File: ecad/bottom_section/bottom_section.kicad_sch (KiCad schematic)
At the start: 13 parts, among them J1 JST PH, J2 JST SH, J3 JST PH, U1 MCP23017_ML

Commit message: Adds a bottom_section board.
It was fast. Seems the right design choices.
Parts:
- removed J1, J3: JST PH, Connector_JST:JST_PH_S4B-PH-K_1x04_P2.00mm_Horizontal, symbol Connector_Generic:Conn_01x04
- added J1, J3: JST PH, Connector_JST:JST_PH_S3B-PH-K_1x03_P2.00mm_Horizontal, symbol Connector_Generic:Conn_01x03
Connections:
- net R6_S6 is gone; now on net R5_SW: U1.18 (GPA1)
- net +5V: now also J1.3 (Pin_3), J3.3 (Pin_3)
- net DIN: now also R8.1, J1.2 (Pin_2); no longer R7.1
- net DOUT: now also R7.1, J3.2 (Pin_2); no longer R8.1
- net GND: now also J1.1 (Pin_1), J3.1 (Pin_1)
- net KeyboardKey_COL1/DIN: no longer R7.2
- net KeyboardKey_COL10/DOUT: now also R7.2
- net KeyboardKey_COL6/DOUT: no longer R8.2
- net R5_SW: no longer U1.17 (GPA0)
- net R6_SW: now also U1.17 (GPA0)
- new net KeyboardKey_COL5/DIN: R8.2
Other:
- moved on the sheet: R7, R8

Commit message: Updates boards
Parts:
- removed R2, R3, R4, R5, R6: 11k, Resistor_SMD:R_0603_1608Metric, symbol Device:R
- added JP1, JP2, JP3: ~, Jumper:SolderJumper-3_P2.0mm_Open_TrianglePad1.0x1.5mm, symbol Jumper:SolderJumper_3_Bridged123
- J1, J3: value JST PH -> JST PH 3; footprint Connector_JST:JST_PH_S3B-PH-K_1x03_P2.00mm_Horizontal -> woodpecker:JST_PH_S3B-PH-SM4-TB_1x03-1MP_P2.00mm_Horizontal
- J2: value JST SH -> JST SH 4; footprint Connector_JST:JST_SH_BM04B-SRSS-TB_1x04-1MP_P1.00mm_Vertical -> woodpecker:JST_SH_BM04B-SRSS-TB_1x04-1MP_P1.00mm_Vertical
- R1: now fitted
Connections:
- net A0: now also JP1.2 (C)
- net A1: now also JP2.2 (C)
- net A2: now also JP3.2 (C); no longer R1.2
- net GND: now also JP1.3 (B), JP2.3 (B), JP3.3 (B)
- new net 3v3_PUP: JP1.1 (A), JP2.1 (A), JP3.1 (A), R1.2

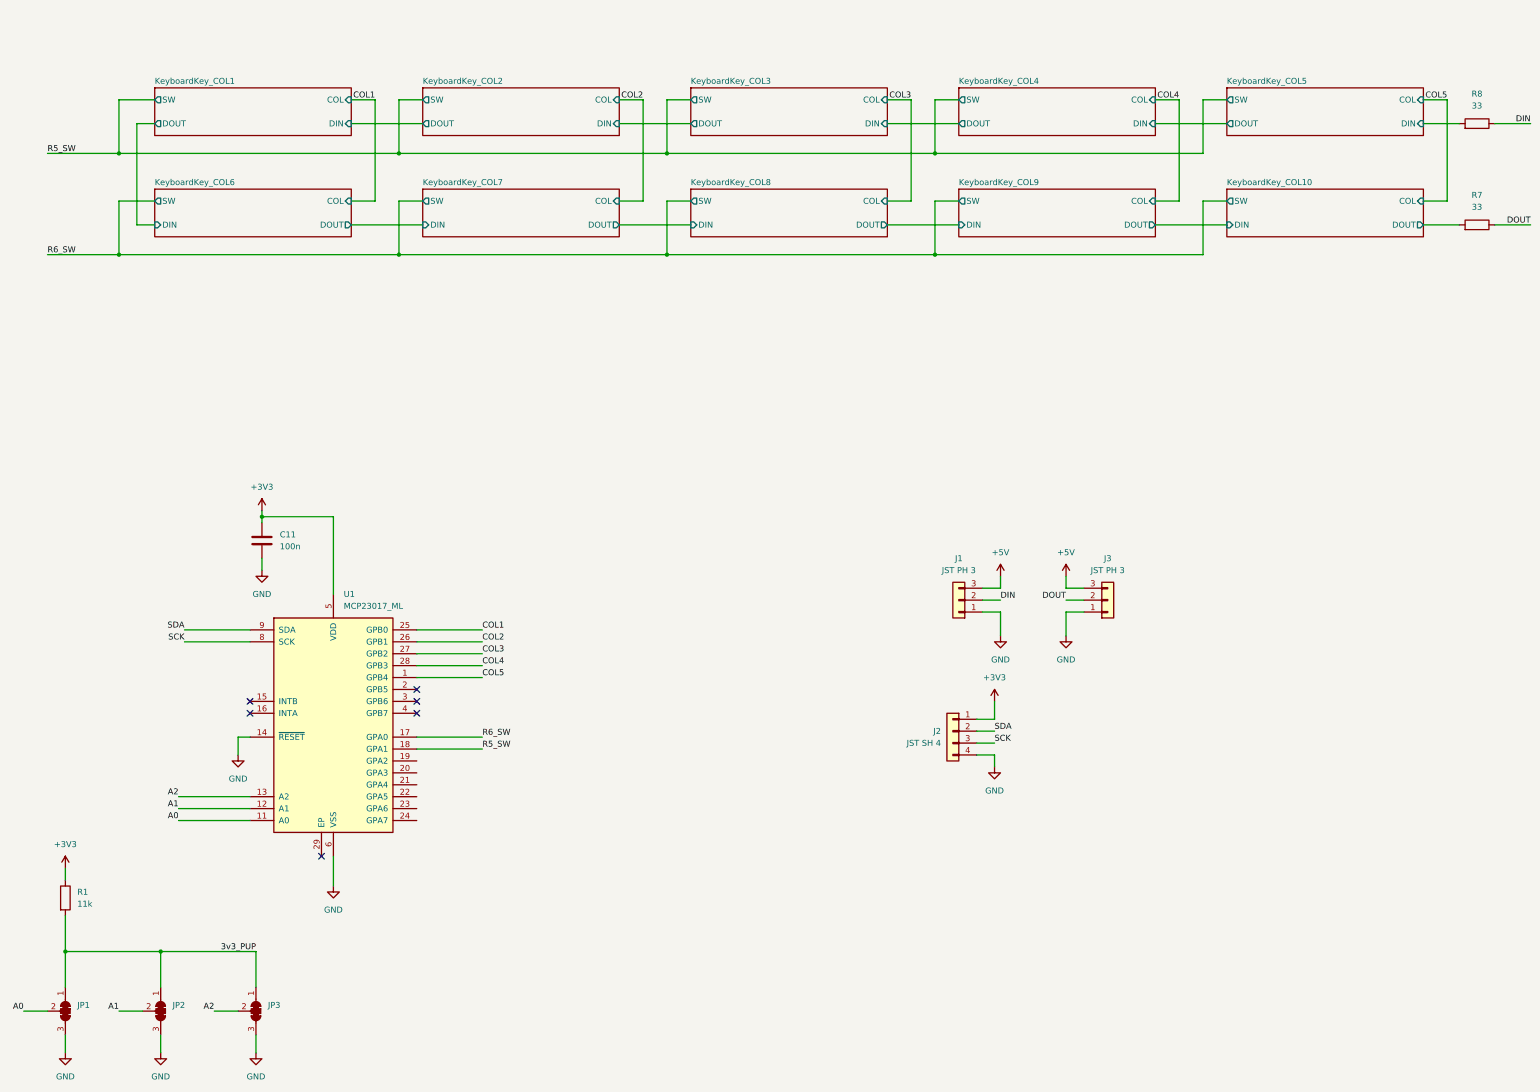
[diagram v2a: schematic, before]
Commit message: Uses Attiny1617 MCU for ADC & Matrix RO
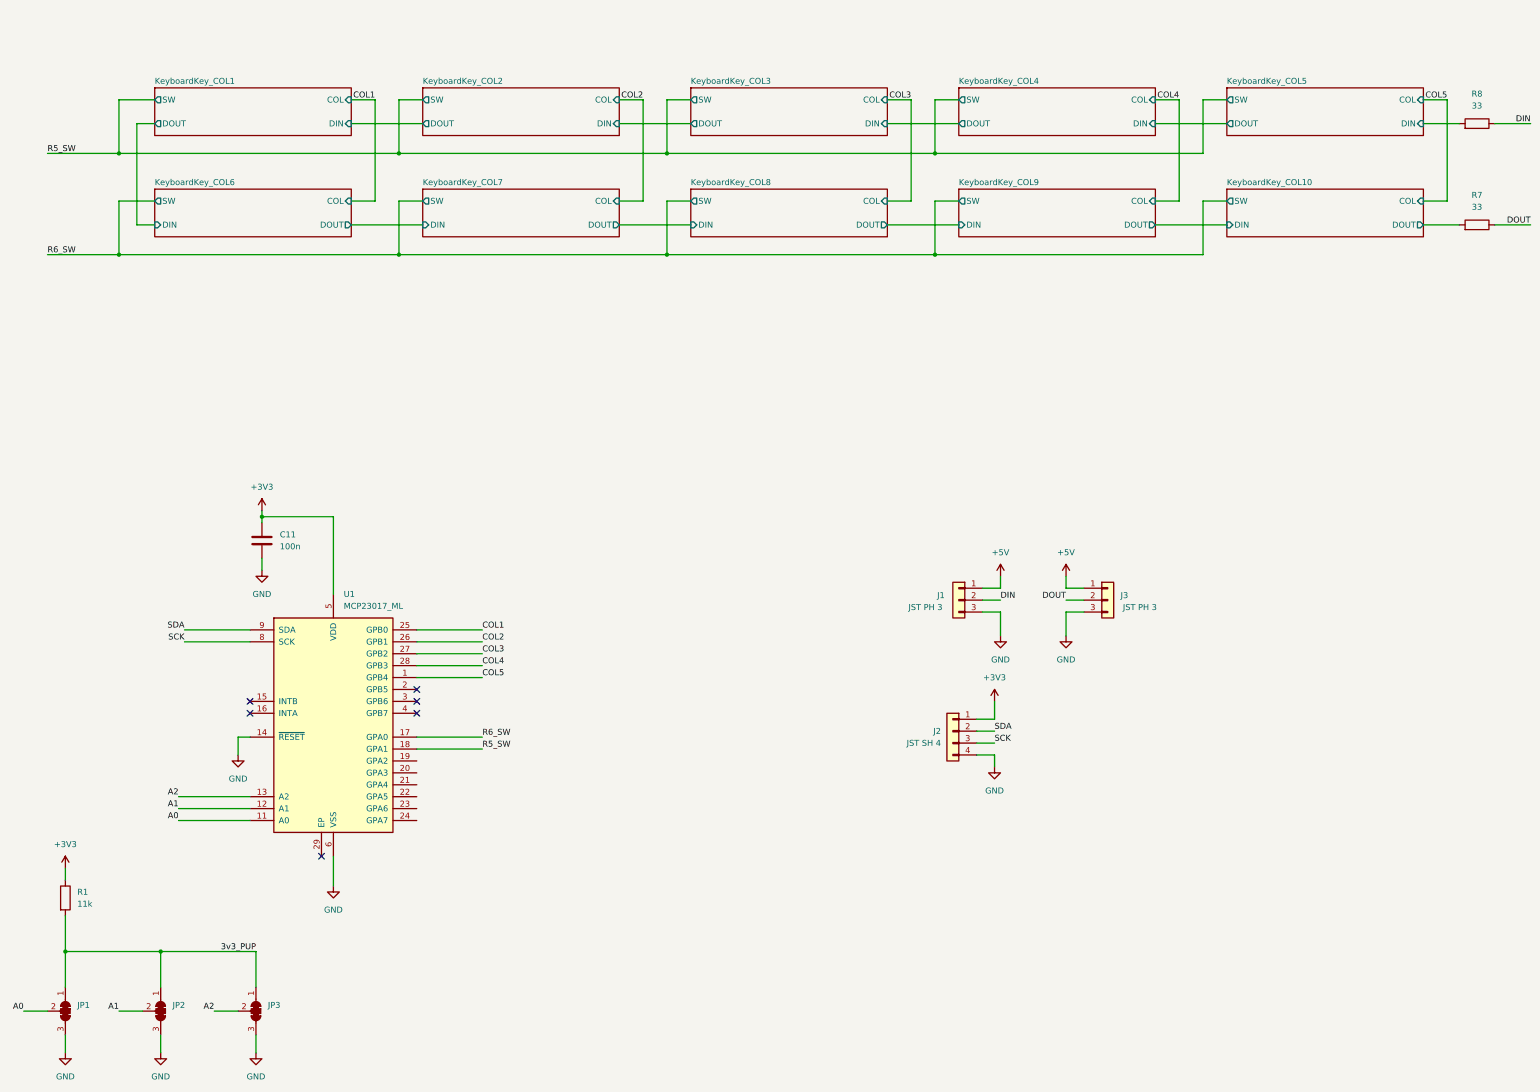
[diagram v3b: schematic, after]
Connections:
- net +5V: now also J1.1 (Pin_1), J3.1 (Pin_1); no longer J1.3 (Pin_3), J3.3 (Pin_3)
- net GND: now also J1.3 (Pin_3), J3.3 (Pin_3); no longer J1.1 (Pin_1), J3.1 (Pin_1)
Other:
- moved on the sheet: J1
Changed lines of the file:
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@@
 (kicad_sch
-	(version 20231120)
+	(version 20250114)
 	(generator "eeschema")
-	(generator_version "8.0")
+	(generator_version "9.0")
 	(paper "A3")
 	(junction
@@
 	(label "COL4"
 		(at 285.75 40.64 180)
-		(fields_autoplaced yes)
 		(effects
 			(font
@@
 	(label "DIN"
 		(at 247.65 147.32 0)
-		(fields_autoplaced yes)
 		(effects
 			(font
@@
 	(label "COL3"
 		(at 228.6 40.64 180)
-		(fields_autoplaced yes)
 		(effects
 			(font
@@
 	(label "DOUT"
 		(at 360.68 67.31 180)
-		(fields_autoplaced yes)
 		(effects
 			(font
@@
 	(label "A1"
 		(at 59.69 234.95 180)
-		(fields_autoplaced yes)
 		(effects
 			(font
@@
 	(label "3v3_PUP"
 		(at 88.9 222.25 180)
-		(fields_autoplaced yes)
 		(effects
 			(font
@@
 	(label "COL4"
 		(at 137.16 161.29 0)
-		(fields_autoplaced yes)
 		(effects
 			(font
@@
 	(label "A2"
 		(at 72.39 189.23 180)
-		(fields_autoplaced yes)
 		(effects
 			(font
@@
 	(label "COL2"
 		(at 171.45 40.64 180)
-		(fields_autoplaced yes)
 		(effects
 			(font
@@
 	(label "R6_SW"
 		(at 137.16 176.53 0)
-		(fields_autoplaced yes)
 		(effects
 			(font
@@
 	(label "R5_SW"
 		(at 137.16 179.07 0)
-		(fields_autoplaced yes)
 		(effects
 			(font
@@
 	(label "SCK"
 		(at 246.38 177.8 0)
-		(fields_autoplaced yes)
 		(effects
 			(font
@@
 	(label "A1"
 		(at 72.39 191.77 180)
-		(fields_autoplaced yes)
 		(effects
 			(font
@@
 	(label "A0"
 		(at 39.37 234.95 180)
-		(fields_autoplaced yes)
 		(effects
 			(font
@@
 	(label "SCK"
 		(at 73.66 156.21 180)
-		(fields_autoplaced yes)
 		(effects
 			(font
@@
 	(label "DOUT"
 		(at 261.62 147.32 180)
-		(fields_autoplaced yes)
 		(effects
 			(font
@@
 	(label "DIN"
 		(at 360.68 45.72 180)
-		(fields_autoplaced yes)
 		(effects
 			(font
@@
 	(label "A2"
 		(at 80.01 234.95 180)
-		(fields_autoplaced yes)
 		(effects
 			(font
@@
 	(label "COL5"
 		(at 342.9 40.64 180)
-		(fields_autoplaced yes)
 		(effects
 			(font
@@
 	(label "R6_SW"
 		(at 44.45 73.66 0)
-		(fields_autoplaced yes)
 		(effects
 			(font
@@
 	(label "R5_SW"
 		(at 44.45 52.07 0)
-		(fields_autoplaced yes)
 		(effects
 			(font
@@
 	(label "A0"
 		(at 72.39 194.31 180)
-		(fields_autoplaced yes)
 		(effects
 			(font
@@
 	(label "COL1"
 		(at 114.3 40.64 180)
-		(fields_autoplaced yes)
 		(effects
 			(font
@@
 	(label "SDA"
 		(at 246.38 175.26 0)
-		(fields_autoplaced yes)
 		(effects
 			(font
@@
 	(label "COL2"
 		(at 137.16 156.21 0)
-		(fields_autoplaced yes)
 		(effects
 			(font
@@
 	(label "COL3"
 		(at 137.16 158.75 0)
-		(fields_autoplaced yes)
 		(effects
 			(font
@@
 	(label "COL1"
 		(at 137.16 153.67 0)
-		(fields_autoplaced yes)
 		(effects
 			(font
@@
 	(label "COL5"
 		(at 137.16 163.83 0)
-		(fields_autoplaced yes)
 		(effects
 			(font
@@
 	(label "SDA"
 		(at 73.66 153.67 180)
-		(fields_autoplaced yes)
 		(effects
 			(font
@@
 		(lib_id "Connector_Generic:Conn_01x03")
 		(at 270.51 147.32 0)
-		(mirror x)
 		(unit 1)
 		(exclude_from_sim no)
@@
 		(on_board yes)
 		(dnp no)
-		(fields_autoplaced yes)
 		(property "Reference" "J3"
-			(at 270.51 138.43 0)
+			(at 274.066 146.304 0)
 			(effects
 				(font
@@
 		)
 		(property "Value" "JST PH 3"
-			(at 270.51 140.97 0)
+			(at 277.368 148.844 0)
 			(effects
 				(font
@@
 	(symbol
 		(lib_id "Connector_Generic:Conn_01x03")
-		(at 238.76 147.32 180)
+		(at 238.76 147.32 0)
+		(mirror y)
 		(unit 1)
 		(exclude_from_sim no)
@@
 		(on_board yes)
 		(dnp no)
-		(fields_autoplaced yes)
 		(property "Reference" "J1"
-			(at 238.76 138.43 0)
+			(at 234.95 146.304 0)
 			(effects
 				(font
@@
 		)
 		(property "Value" "JST PH 3"
-			(at 238.76 140.97 0)
+			(at 231.648 148.844 0)
 			(effects
 				(font
@@
 		(at 238.76 59.69)
 		(size 41.91 10.16)
+		(exclude_from_sim no)
+		(in_bom yes)
+		(on_board yes)
+		(dnp no)
 		(fields_autoplaced yes)
 		(stroke
@@
 		(at 238.76 38.1)
 		(size 41.91 10.16)
+		(exclude_from_sim no)
+		(in_bom yes)
+		(on_board yes)
+		(dnp no)
 		(fields_autoplaced yes)
 		(stroke
@@
 		(at 295.91 59.69)
 		(size 41.91 10.16)
+		(exclude_from_sim no)
+		(in_bom yes)
+		(on_board yes)
+		(dnp no)
 		(fields_autoplaced yes)
 		(stroke
@@
 		(at 67.31 59.69)
 		(size 41.91 10.16)
+		(exclude_from_sim no)
+		(in_bom yes)
+		(on_board yes)
+		(dnp no)
 		(fields_autoplaced yes)
 		(stroke
@@
 		(at 124.46 38.1)
 		(size 41.91 10.16)
+		(exclude_from_sim no)
+		(in_bom yes)
+		(on_board yes)
+		(dnp no)
 		(fields_autoplaced yes)
 		(stroke
@@
 		(at 181.61 59.69)
 		(size 41.91 10.16)
+		(exclude_from_sim no)
+		(in_bom yes)
+		(on_board yes)
+		(dnp no)
 		(fields_autoplaced yes)
 		(stroke
@@
 		(at 181.61 38.1)
 		(size 41.91 10.16)
+		(exclude_from_sim no)
+		(in_bom yes)
+		(on_board yes)
+		(dnp no)
 		(fields_autoplaced yes)
 		(stroke
@@
 		(at 295.91 38.1)
 		(size 41.91 10.16)
+		(exclude_from_sim no)
+		(in_bom yes)
+		(on_board yes)
+		(dnp no)
 		(fields_autoplaced yes)
 		(stroke
@@
 		(at 124.46 59.69)
 		(size 41.91 10.16)
+		(exclude_from_sim no)
+		(in_bom yes)
+		(on_board yes)
+		(dnp no)
 		(fields_autoplaced yes)
 		(stroke
@@
 		(at 67.31 38.1)
 		(size 41.91 10.16)
+		(exclude_from_sim no)
+		(in_bom yes)
+		(on_board yes)
+		(dnp no)
 		(fields_autoplaced yes)
 		(stroke
@@
 		)
 	)
+	(embedded_fonts no)
 )

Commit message: Uses attiny16176
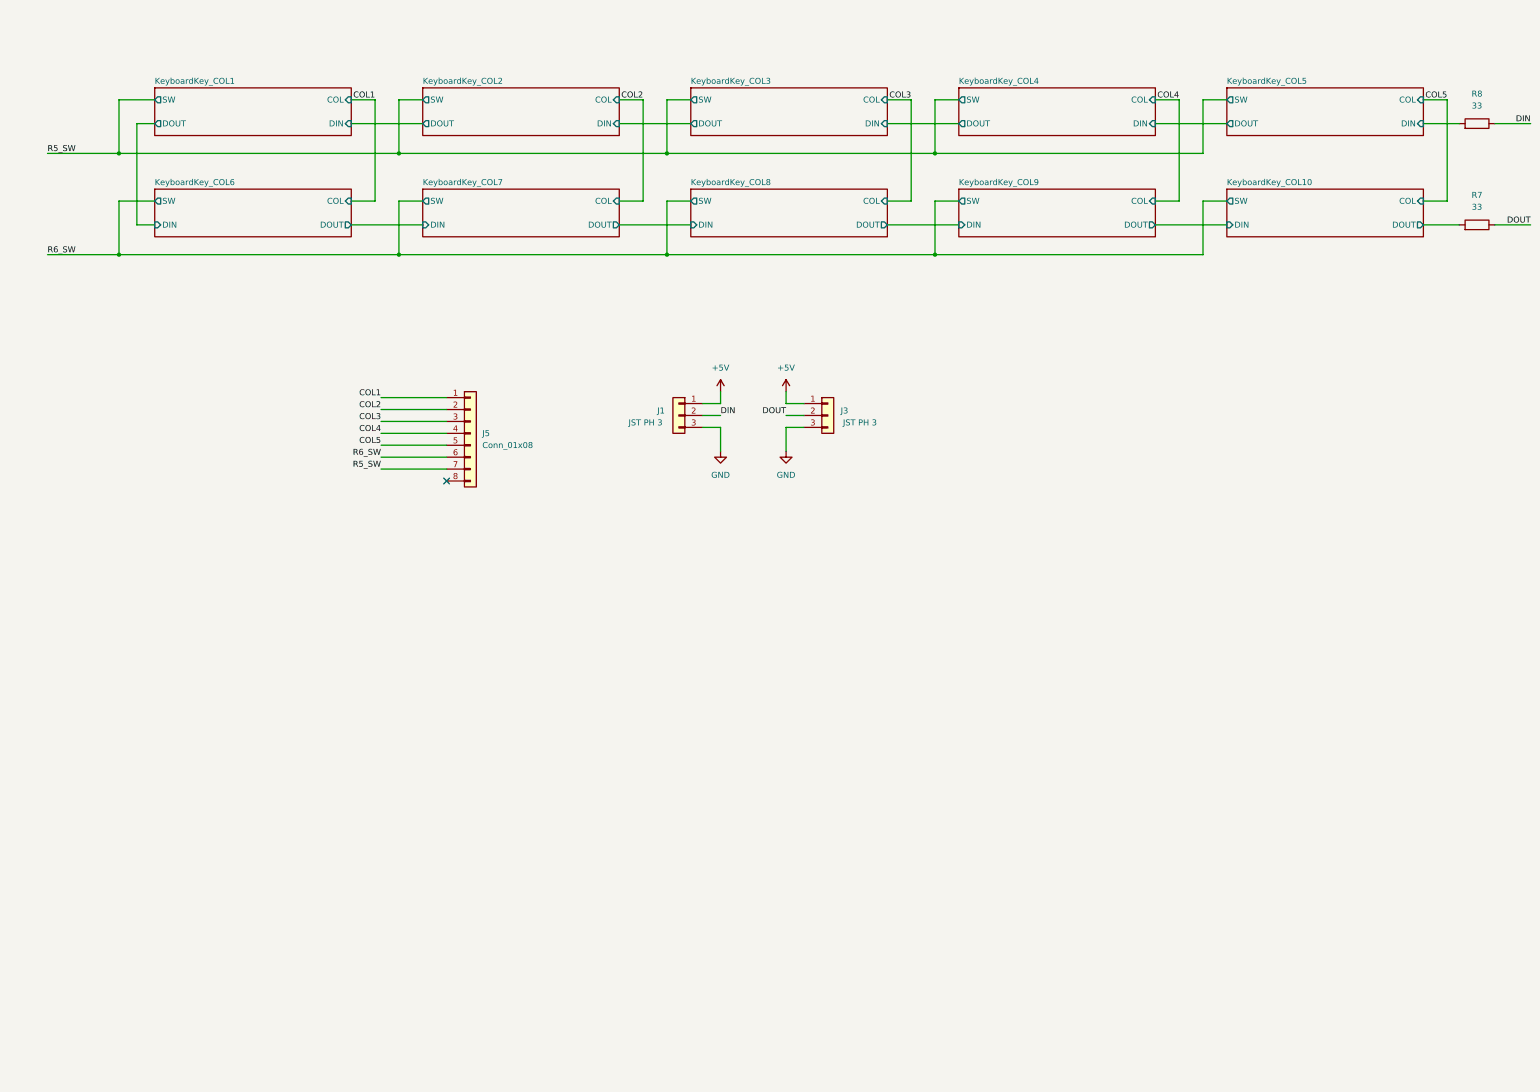
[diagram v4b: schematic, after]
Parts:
- removed C11: 100n, Capacitor_SMD:C_0603_1608Metric, symbol Device:C
- removed J2: JST SH 4, woodpecker:JST_SH_BM04B-SRSS-TB_1x04-1MP_P1.00mm_Vertical, symbol Connector_Generic:Conn_01x04
- removed JP1, JP2, JP3: ~, Jumper:SolderJumper-3_P2.0mm_Open_TrianglePad1.0x1.5mm, symbol Jumper:SolderJumper_3_Bridged123
- removed R1: 11k, Resistor_SMD:R_0603_1608Metric, symbol Device:R
- removed U1: MCP23017_ML, Package_DFN_QFN:QFN-28-1EP_6x6mm_P0.65mm_EP4.25x4.25mm, symbol Interface_Expansion:MCP23017_ML
- added J5: Conn_01x08, Connector_TE-Connectivity:TE_Micro-MaTch_215079-8_2x04_P1.27mm_Vertical, symbol Connector_Generic:Conn_01x08
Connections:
- net COL1: now also J5.1 (Pin_1)
- net COL2: now also J5.2 (Pin_2)
- net COL3: now also J5.3 (Pin_3)
- net COL4: now also J5.4 (Pin_4)
- net COL5: now also J5.5 (Pin_5)
- net R5_SW: now also J5.7 (Pin_7)
- net R6_SW: now also J5.6 (Pin_6)
- no-connect marks 6 -> 1
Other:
- moved on the sheet: J1, J3
